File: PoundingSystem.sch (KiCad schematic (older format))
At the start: 137 parts, among them J1 USB_B_Micro, J2 LINE OUT, J3 MICROPHONE, J4 LINE IN, J5 HEADPHONES, J6 Debug, SW1 Rotary_Encoder_Switch, SW2 Rotary_Encoder, SW3 Rotary_Encoder, SW4 Rotary_Encoder, SW5 SW_SPST, SW6 SW_SPST, SW7 SW_SPST, SW8 Rotary_Encoder, SW9 SW_SPDT, U1 AMS1117-3.3, U10 SN74LVC2G34, U11 SN74LVC2G34, U12 SN74LVC2G34, U2 STM32F405RGT6, U3 USBLC6-2SC6, U4 SN74LVC2G34, U5 Nokia_5110_LCD, U6 SN74LVC2G34, U7 WM8978CGEFL_RV, U8 SN74LVC2G34, U9 SN74LVC2G34

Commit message: h7 version;
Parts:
- removed C10, C11, C28, C36, C39, C40, C53: 100nf, Capacitor_SMD:C_0402_1005Metric, symbol Device:C_Small
- removed C50: 10nf, Capacitor_SMD:C_0402_1005Metric, symbol Device:C_Small
- removed R28: 10k, Resistor_SMD:R_0402_1005Metric, symbol Device:R_Small
- removed SW6: SW_SPST, Button_Switch_THT:SW_PUSH_6mm_H4.3mm, symbol Switch:SW_SPST
- removed U12, U4, U6, U8, U9: SN74LVC2G34, Package_TO_SOT_SMD:SOT-23-6, symbol RocketScreamKicadLibrary:SN74LVC2G34
- removed U2: STM32F405RGT6, Package_QFP:LQFP-64_10x10mm_P0.5mm, symbol MCU_ST_STM32F4:STM32F405RGTx
- added C58: 4.7u, Capacitor_SMD:C_0603_1608Metric, symbol Device:C_Small
- added C59, C60, C61, C62, C63, C64, C65, C66, C67: 100nf, Capacitor_SMD:C_0402_1005Metric, symbol Device:C_Small
- added D8: LED_BPM, LED_SMD:LED_0805_2012Metric, symbol Device:LED
- added R34, R35, R37: 10k, Resistor_SMD:R_0402_1005Metric, symbol Device:R_Small
- added R36: 0, Resistor_SMD:R_0402_1005Metric, symbol Device:R_Small
- added U13: STM32H743IITx, Package_QFP:LQFP-176_24x24mm_P0.5mm, symbol MCU_ST_STM32H7:STM32H743IITx
- added U2: CAT24C256, Package_SO:SOIC-8-1EP_3.9x4.9mm_P1.27mm_EP2.29x3mm, symbol Memory_EEPROM:CAT24C256
- C3: value 10u -> 100nf; footprint Capacitor_SMD:C_0603_1608Metric -> Capacitor_SMD:C_0402_1005Metric; LCSC Part # C19702 -> C1525
- R5: value 2k2 -> 10k; LCSC Part # C25879 -> C25744
- R6: value 2k2 -> 180; footprint Resistor_SMD:R_0402_1005Metric -> Resistor_SMD:R_0603_1608Metric; LCSC Part # C25879 -> C22828
- U10, U11: symbol RocketScreamKicadLibrary:SN74LVC2G34 -> PoundingSystem-rescue:SN74LVC2G34-RocketScreamKicadLibrary
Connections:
- net +3.3VA: now also R36.2, U13.39 (VDDA)
- net +3V3: now also C12.2, C3.2, C4.2, C5.2, C6.2, C7.2, C8.2, R5.2, C58.2, C59.2, C60.2, C61.2, C62.2, C63.2, C64.2, C65.2, C66.2, C67.2, R34.2, R35.2, R37.2, U13.103 (VDD), U13.114 (VDD33_USB), U13.127 (VDD), U13.136 (VDD), U13.149 (VDD), U13.15 (VDD), U13.159 (VDD), U13.172 (VDD), U13.23 (VDD), U13.36 (VDD), U13.49 (VDD), U13.6 (VBAT), U13.62 (VDD), U13.72 (VDD), U13.82 (VDD), U13.91 (VDD), U2.8 (VCC); no longer C12.1, C3.1, C4.1, C5.1, C6.1, C7.1, C8.1, R5.1, R6.1
- net +5V: now also SW9.3 (C); no longer SW9.2 (B)
- net BOOT0: now also U13.166 (BOOT0)
- net FIRE_BTN: now also U13.64 (PF14)
- net FIRE_LED: now also U13.65 (PF15)
- net GND: now also C12.1, C3.1, C4.1, C5.1, C6.1, C7.1, C8.1, C58.1, C59.1, C60.1, C61.1, C62.1, C63.1, C64.1, C65.1, C66.1, C67.1, D8.1 (K), U13.102 (VSS), U13.113 (VSS), U13.126 (VSS), U13.135 (VSS), U13.14 (VSS), U13.148 (VSS), U13.158 (VSS), U13.22 (VSS), U13.37 (VSSA), U13.48 (VSS), U13.61 (VSS), U13.71 (VSS), U13.90 (VSS), U2.1 (A0), U2.2 (A1), U2.3 (A2), U2.4 (GND); no longer C12.2, C3.2, C4.2, C5.2, C6.2, C7.2, C8.2
- net HOLD_SW: now also U13.56 (PB0)
- net HSE_IN: now also U13.29 (PH0)
- net HSE_OUT: now also U13.30 (PH1)
- net I2C2_SCL: now also U13.17 (PF1); no longer R5.2
- net I2C2_SDA: now also U13.16 (PF0); no longer R6.2
- net I2S2_MCK: now also U13.54 (PC4)
- net I2S2_SCLK: now also U13.51 (PA5)
- net I2S2_SDI: now also U13.152 (PG9)
- net I2S2_SDO: now also U13.151 (PD7)
- net I2S2_WS: now also U13.50 (PA4)
- net LCD_CS: now also U13.175 (PI6)
- net LCD_DC: now also U13.176 (PI7)
- net NRST: now also U13.31 (NRST)
- net SPI3_MOSI: now also U13.5 (PE6)
- net SPI3_SCK: now also U13.1 (PE2)
- net SW1_A: now also R29.1, U13.115 (PC6)
- net SW1_B: now also R30.1, U13.116 (PC7)
- net SW1_BTN: now also U13.143 (PD1)
- net SWCLK: now also U13.137 (PA14)
- net SWDIO: now also U13.124 (PA13)
- net SWO: now also U13.161 (PB3)
- net TIM1_CH1: now also R19.1, U13.70 (PE9)
- net TIM1_CH2: now also R20.1, U13.74 (PE11)
- net TIM3_CH1: now also R18.1, U13.53 (PA7)
- net TIM3_CH2: now also R17.1, U13.52 (PA6)
- net TIM4_CH1: now also R24.1, U13.100 (PD12)
- net TIM4_CH2: now also R22.1, U13.101 (PD13)
- net USB_D+: now also U13.123 (PA12)
- net USB_D-: now also U13.122 (PA11)
- net at C15.2: now also U13.81 (VCAP1)
- net at C16.2: now also U13.125 (VCAP2)
- net at D2.2 (A): now also SW9.2 (B); no longer SW9.1 (A)
- net at C49.2, R27.2, SW1.S2: now also R5.1
- net at C47.2, R26.2, SW5.2 (B): now also R35.1
- net TIM5_CH2: now reaches R21.1
- net TIM5_CH2: now also U13.87 (PH10)
- net TIM5_CH1: now reaches R23.1
- net TIM5_CH1: now also U13.88 (PH11)
- net at C46.2, R25.2, SW7.2 (B): now also R34.1
- net BACK_BTN: no longer names the net of U11.4 (2Y)
- net LCD_BL renamed LCD_BL1
- net LCD_BL1: now also U13.132 (PI1); no longer R16.2, R3.2
- new net: R37.1, U13.171 (PDR_ON)
- new net: R36.1, U13.38 (VREF+)
- new net: D8.2 (A), R6.1
- new net EEP_WP: U13.145 (PD3), U2.7 (WP)
- new net I2C1_SCL: U13.164 (PB6), U2.6 (SCL)
- new net I2C1_SDA: U13.165 (PB7), U2.5 (SDA)
- new net LCD_BL2: R16.2, R3.2, U13.45 (PH4)
- new net LED_BPM: R6.2, U13.144 (PD2)
- no-connect marks 29 -> 11
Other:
- moved on the sheet: C1, C13, C14, C15, C16, C17, C18, C19, C2, C20, C21, C22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

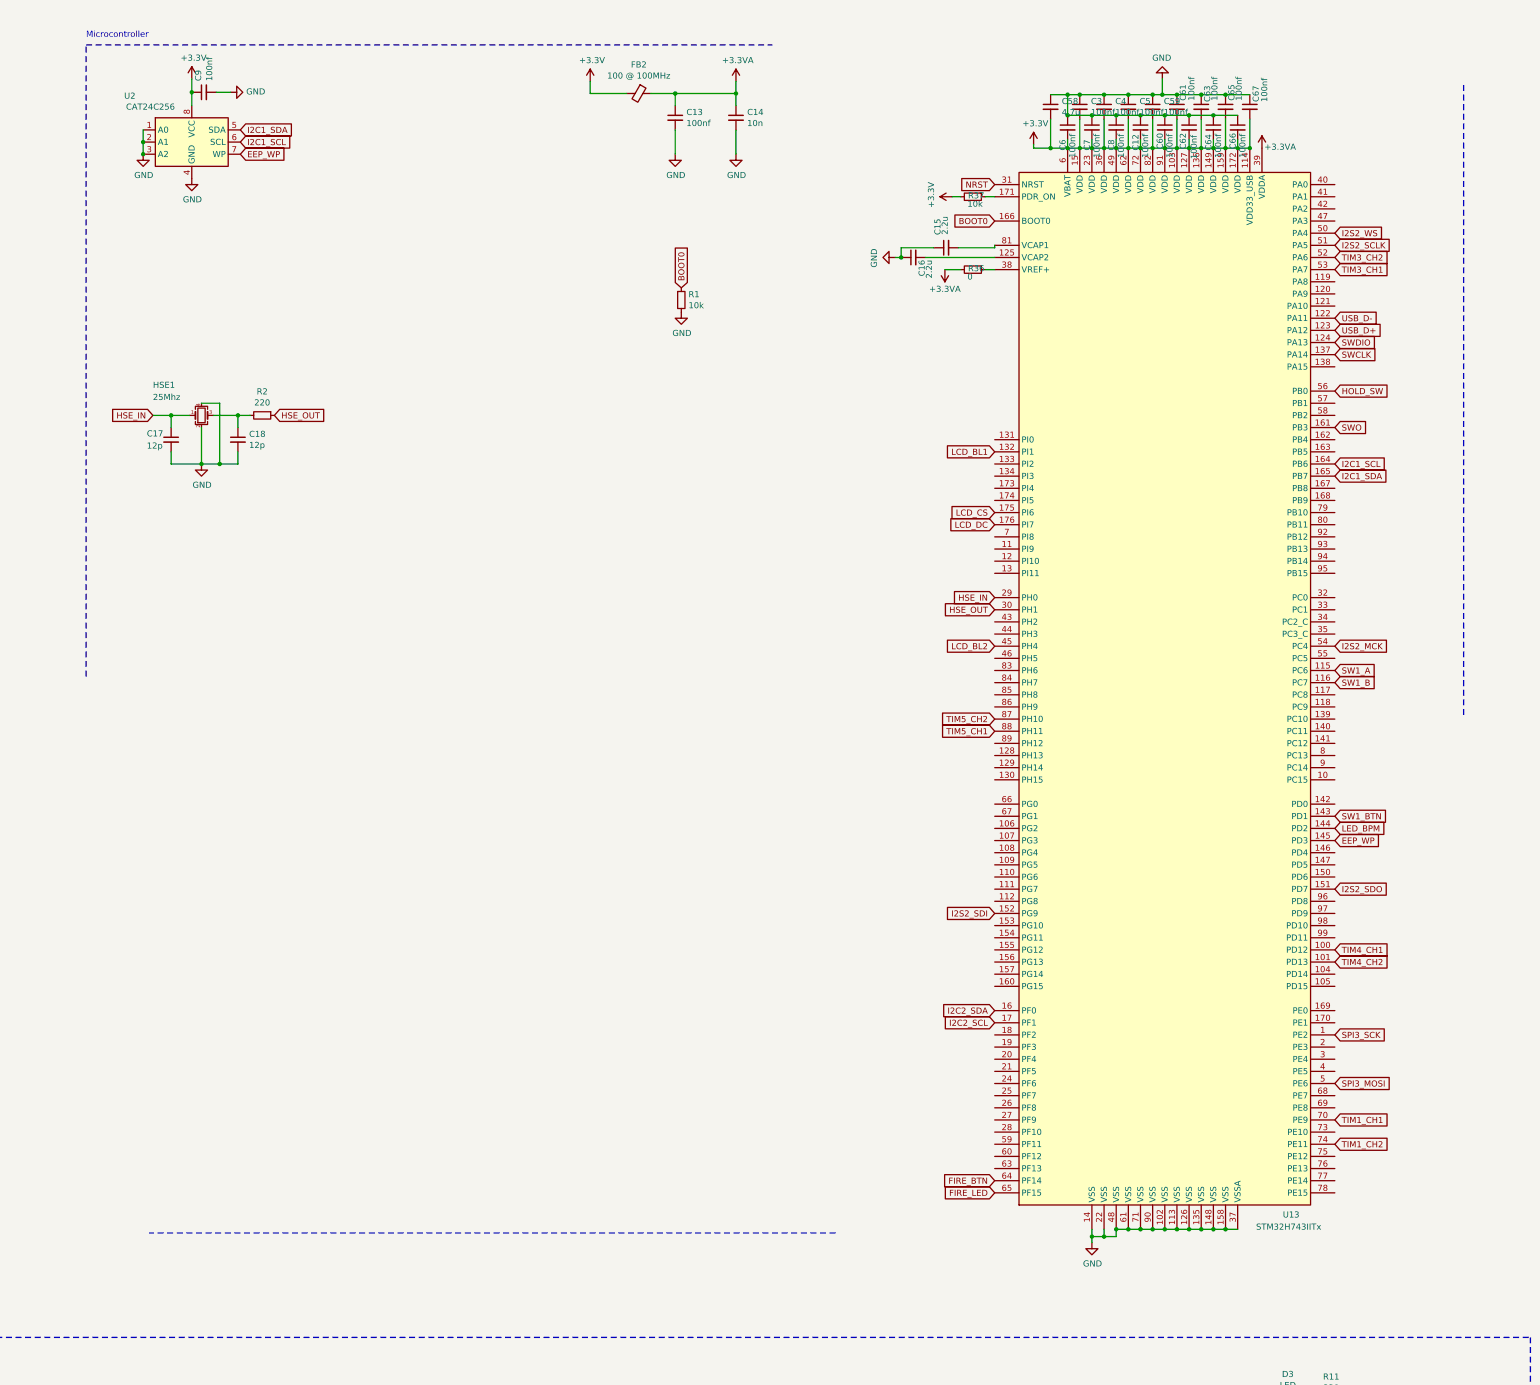
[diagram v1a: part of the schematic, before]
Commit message: switch MPU to stm32h7
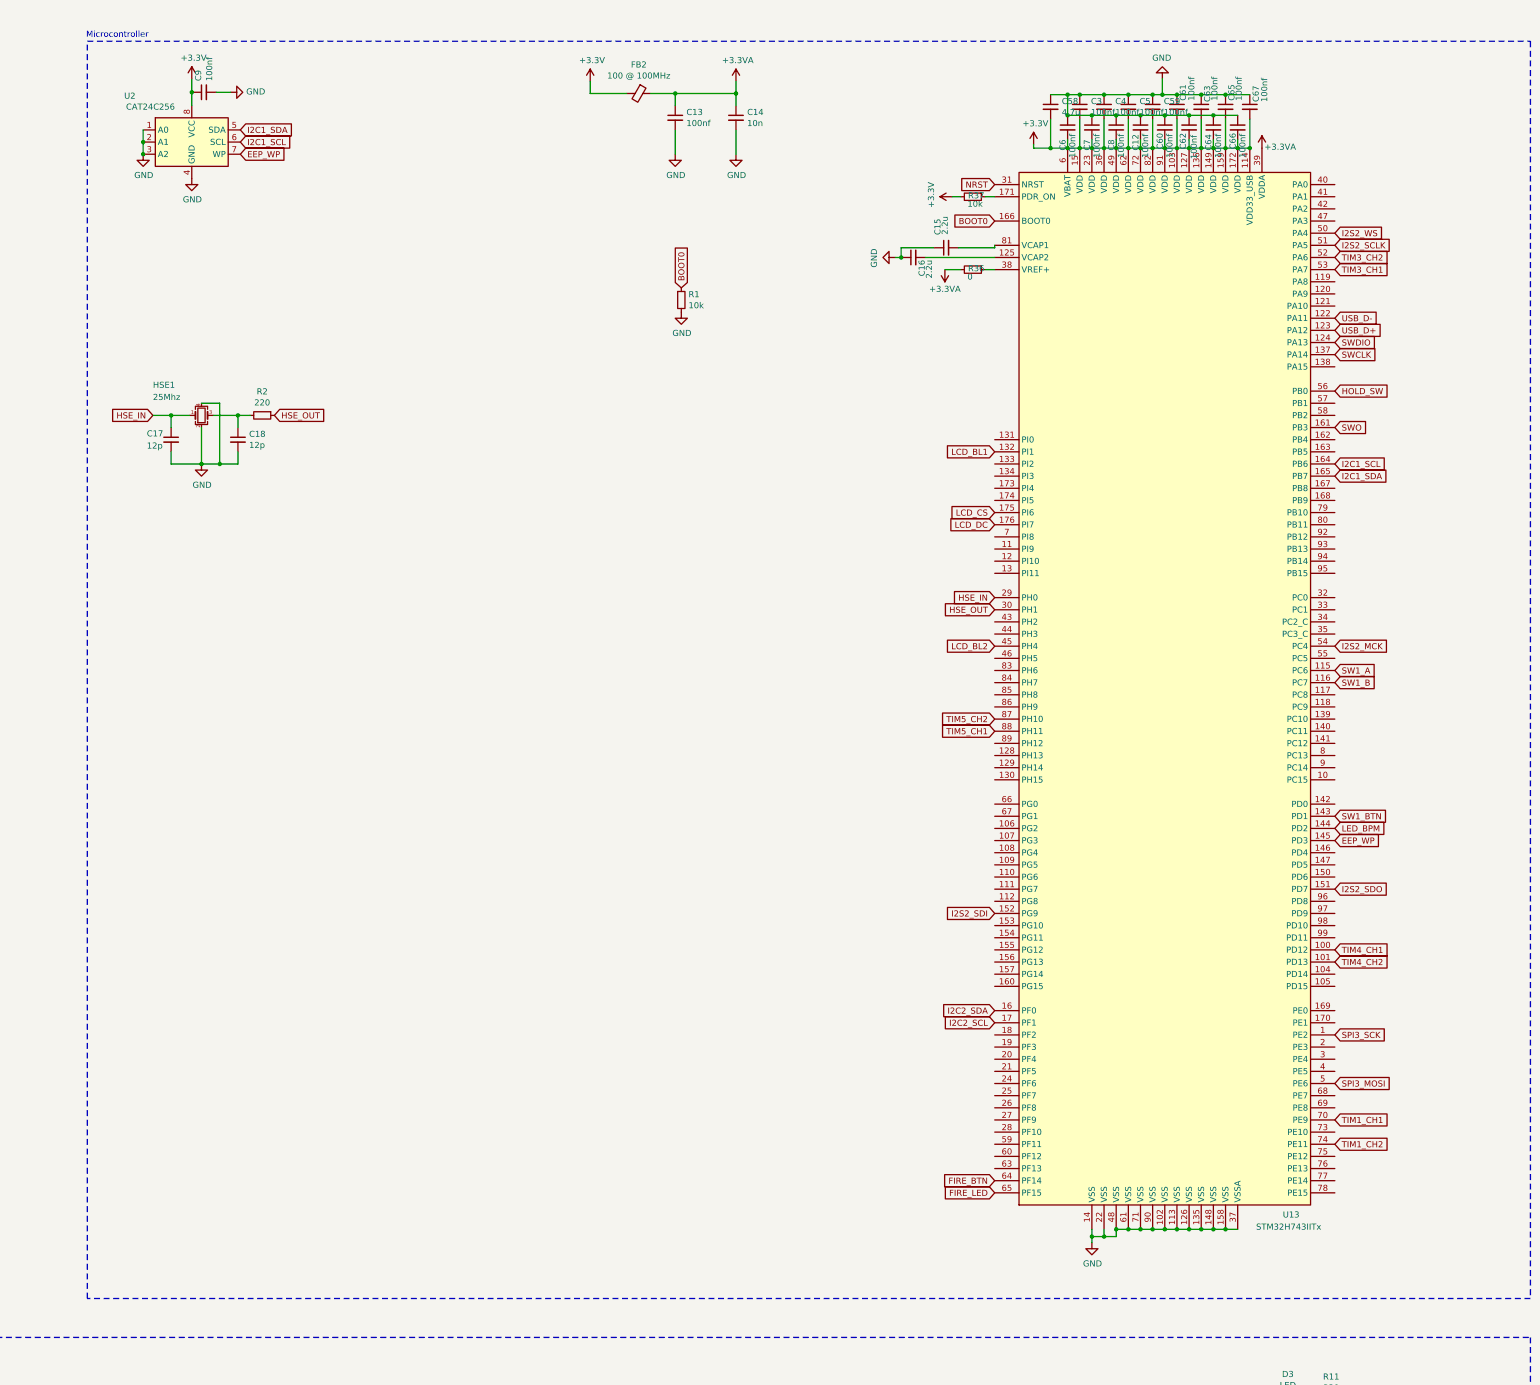
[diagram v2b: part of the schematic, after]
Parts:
- U13: LCSC Part # (none) -> C89597
- U3: LCSC Part # C558442 -> C7519
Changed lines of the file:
@@
 	0    -1   -1   0
 $EndComp
-Wire Notes Line
-	10520 1010 16170 1010
-Wire Notes Line
-	21860 1340 21860 6540
-Wire Notes Line
-	16690 10790 11040 10790
-Wire Notes Line
-	10520 6210 10520 1010
 Text Notes 10520 960  0    50   ~ 0
 Microcontroller
@@
 F 2 "Package_TO_SOT_SMD:SOT-23-6" H 3430 3465 50  0001 C CNN
 F 3 "https://www.st.com/resource/en/datasheet/usblc6-2.pdf" H 3630 4315 50  0001 C CNN
-F 4 "C558442" H 3430 3965 50  0001 C CNN "LCSC Part #"
+F 4 "C7519" H 3430 3965 50  0001 C CNN "LCSC Part #"
 	1    3430 3965
 	1    0    0    -1
@@
 F 2 "Package_QFP:LQFP-176_24x24mm_P0.5mm" H 18200 1960 50  0001 R CNN
 F 3 "http://www.st.com/st-web-ui/static/active/en/resource/technical/document/datasheet/DM00387108.pdf" H 19400 6260 50  0001 C CNN
+F 4 "C89597" H 19400 6260 50  0001 C CNN "LCSC Part #"
 	1    19400 6260
 	1    0    0    -1
@@
 $EndComp
 Connection ~ 10990 1910
+Wire Notes Line
+	22410 980  22410 11330
+Wire Notes Line
+	22410 11330 10530 11330
+Wire Notes Line
+	10530 11330 10530 980
+Wire Notes Line
+	10530 980  22410 980
 $EndSCHEMATC

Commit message: production: generate production files
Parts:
- U10, U11: footprint Package_TO_SOT_SMD:SOT-23-6 -> Package_TO_SOT_SMD:SOT-363_SC-70-6
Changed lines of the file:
@@
 F 0 "U10" H 20810 13487 60  0000 C CNN
 F 1 "SN74LVC2G34" H 20810 13381 60  0000 C CNN
-F 2 "Package_TO_SOT_SMD:SOT-23-6" H 20810 12550 60  0001 C CNN
+F 2 "Package_TO_SOT_SMD:SOT-363_SC-70-6" H 20810 12550 60  0001 C CNN
 F 3 "" H 20860 12900 60  0000 C CNN
 F 4 "C14461" H 20810 13000 50  0001 C CNN "LCSC Part #"
@@
 F 0 "U11" H 6140 13527 60  0000 C CNN
 F 1 "SN74LVC2G34" H 6140 13421 60  0000 C CNN
-F 2 "Package_TO_SOT_SMD:SOT-23-6" H 6140 12590 60  0001 C CNN
+F 2 "Package_TO_SOT_SMD:SOT-363_SC-70-6" H 6140 12590 60  0001 C CNN
 F 3 "" H 6190 12940 60  0000 C CNN
 F 4 "C14461" H 6140 13040 50  0001 C CNN "LCSC Part #"

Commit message: fix: update schematic labels
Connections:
- net SPI3_MOSI renamed SPI4_MOSI
- net SPI3_SCK renamed SPI4_SCK
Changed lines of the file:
@@
 TIM5_CH2
 Text GLabel 7510 1970 0    50   Input ~ 0
-SPI3_MOSI
+SPI4_MOSI
 Text GLabel 7510 2070 0    50   Input ~ 0
-SPI3_SCK
+SPI4_SCK
 $Comp
 L Device:C_Small C21
@@
 HOLD_SW
 Text GLabel 20800 9160 2    50   Input ~ 0
-SPI3_SCK
+SPI4_SCK
 Text GLabel 20800 9560 2    50   Input ~ 0
-SPI3_MOSI
+SPI4_MOSI
 $Comp
 L Device:C_Small C59
